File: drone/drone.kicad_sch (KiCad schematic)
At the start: 59 parts, among them Q1 AO3400A, U2 MPU-6050, U3 MP2303ADN

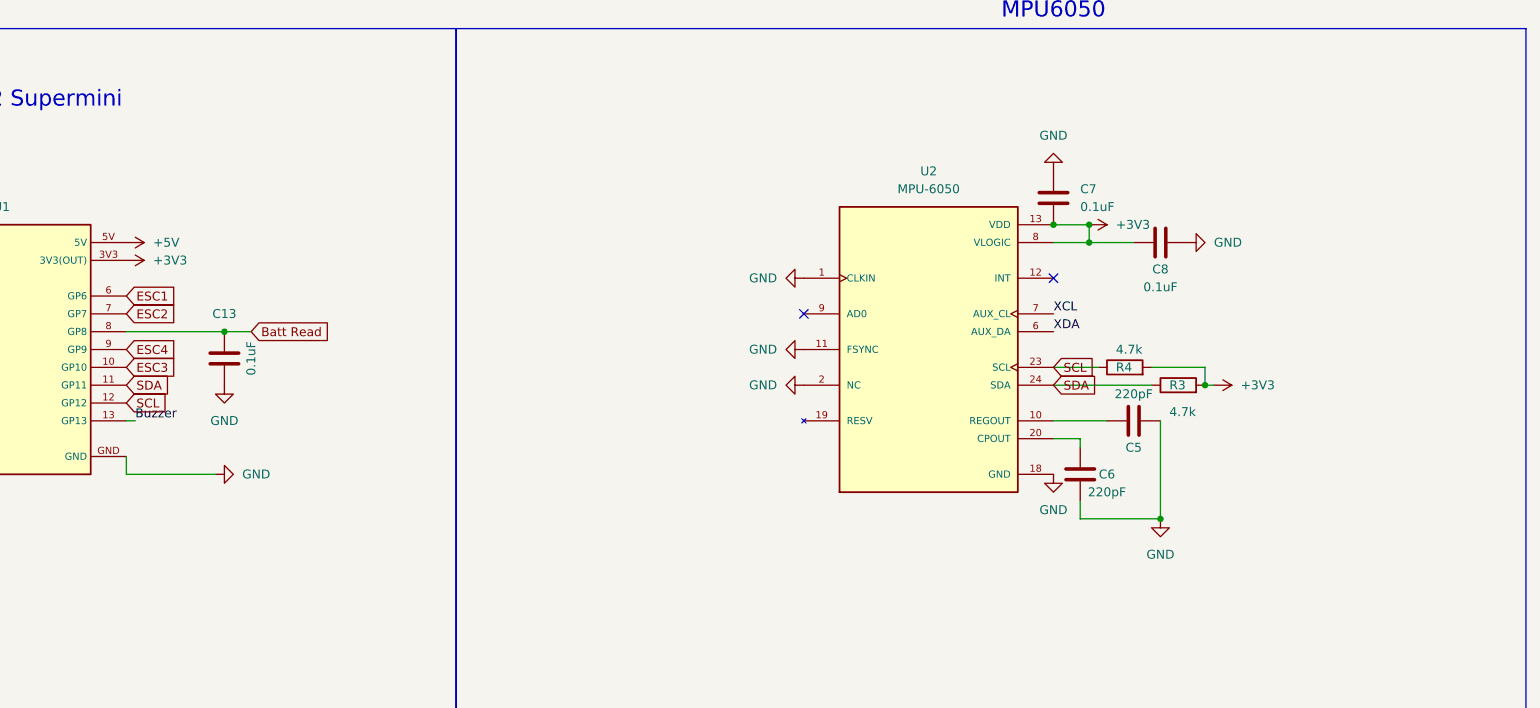
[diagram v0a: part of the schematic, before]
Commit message: add ldo ams1117 3.3v
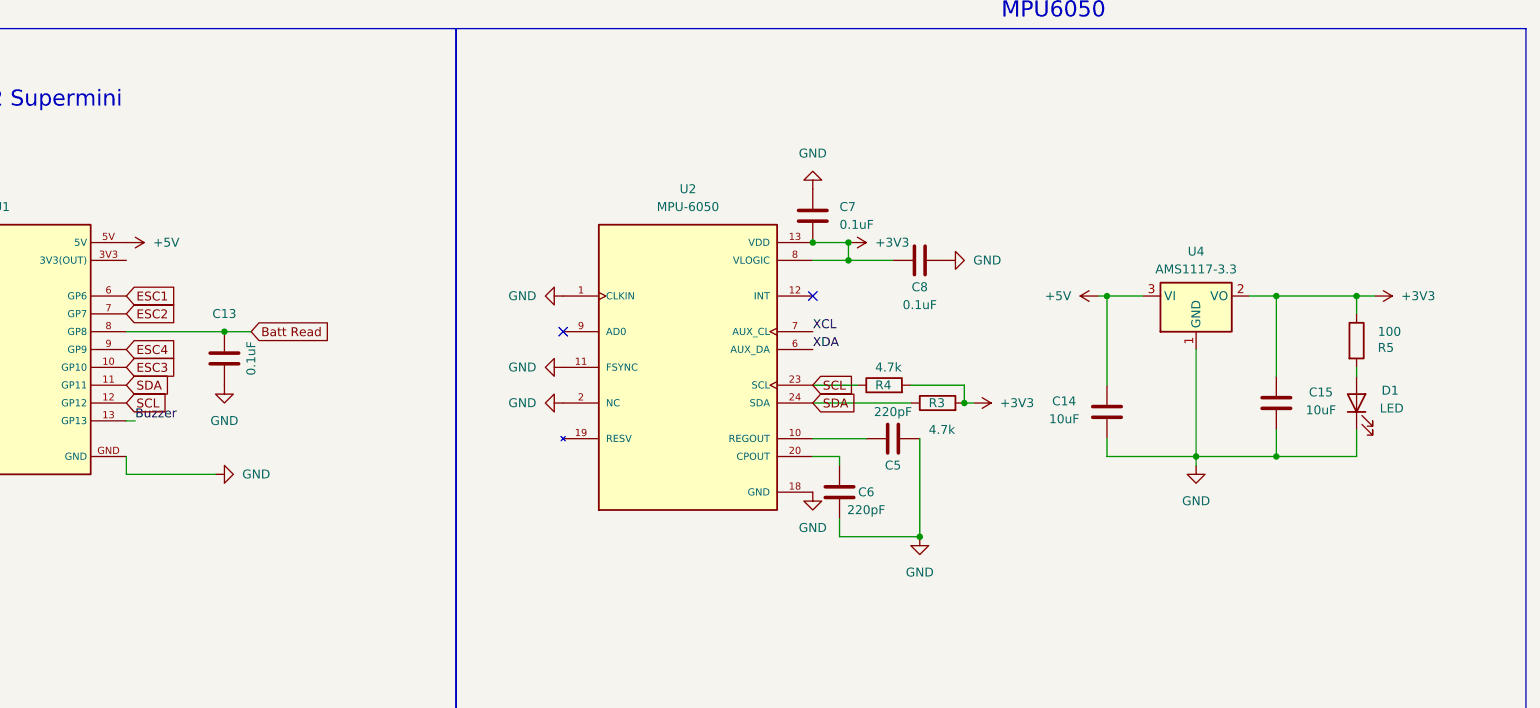
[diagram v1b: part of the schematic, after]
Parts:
- added C14, C15: 10uF, Capacitor_SMD:C_0805_2012Metric_Pad1.18x1.45mm_HandSolder, symbol Device:C
- added D1: LED, LED_SMD:LED_0603_1608Metric, symbol Device:LED
- added R5: 100, Resistor_SMD:R_0805_2012Metric_Pad1.20x1.40mm_HandSolder, symbol Device:R
- added U4: AMS1117-3.3, Package_TO_SOT_SMD:SOT-223-3_TabPin2, symbol Regulator_Linear:AMS1117-3.3
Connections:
- net +3V3: now also C15.2, R5.1, U4.2 (VO); no longer U1.3V3 (3V3(OUT))
- net +5V: now also C14.2, U4.3 (VI)
- net GND: now also C14.1, C15.1, D1.1 (K), U4.1 (GND)
- new net: D1.2 (A), R5.2
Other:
- moved on the sheet: C5, C6, C7, C8, R3, R4, U2

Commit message: 6/6
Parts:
- added CP1: 470uF, symbol Device:C_Polarized
- added TP13, TP14, TP15, TP16, TP17: TestPoint, TestPoint:TestPoint_Pad_D1.0mm, symbol Connector:TestPoint
- C10: value 10nF -> 100nF
- C12: value 22nF -> 10uF
- C5: value 220pF -> 0.1uF
- C6: value 220pF -> 2.2nF
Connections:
- net +3V3: no longer +Buzzer1.1
- net +5V: now also +Buzzer1.1, TP13.1, TP14.1
- net GPIO3: now reaches U1.3 (GP3)
- net GPIO3: now also TP16.1
- net GPIO4: now reaches U1.4 (GP4)
- net GPIO4: now also TP15.1
- net GPIO5: now reaches U1.5 (GP5)
- net GPIO5: now also TP17.1
- no-connect marks 2 -> 3
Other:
- note added: "GPIO"
- note added: "i2c"
- note removed: "EXTEND I2C"
- moved on the sheet: +Buzzer1, -Buzzer1, Q1, TP19, TP2
